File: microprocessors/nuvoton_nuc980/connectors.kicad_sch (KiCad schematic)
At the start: 9 parts, among them J10 Pmod UART 1x06 socket, J12 Pmod GPIO 1x06 socket, J13 Pmod GPIO 2x06 socket, J4 Pmod UART 1x06 socket, J5 Pmod SPI 1x06 socket, J6 Pmod GPIO 2x06 socket, J7 Pmod I2S 2x06 socket, J8 Pmod I2C 1x06 socket, J9 Conn_01x10

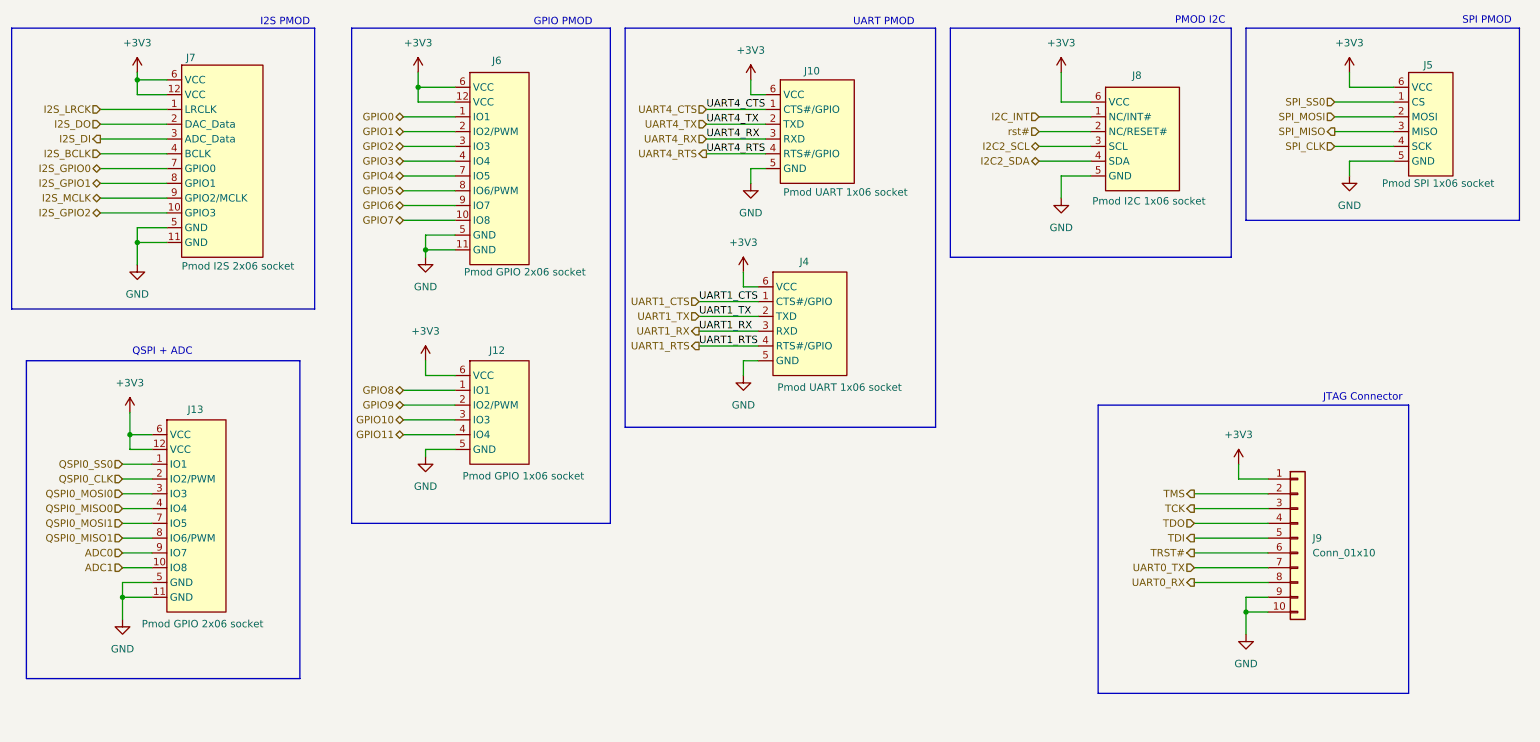
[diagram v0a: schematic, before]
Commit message: feat: ERC passing cotti-nuvoton
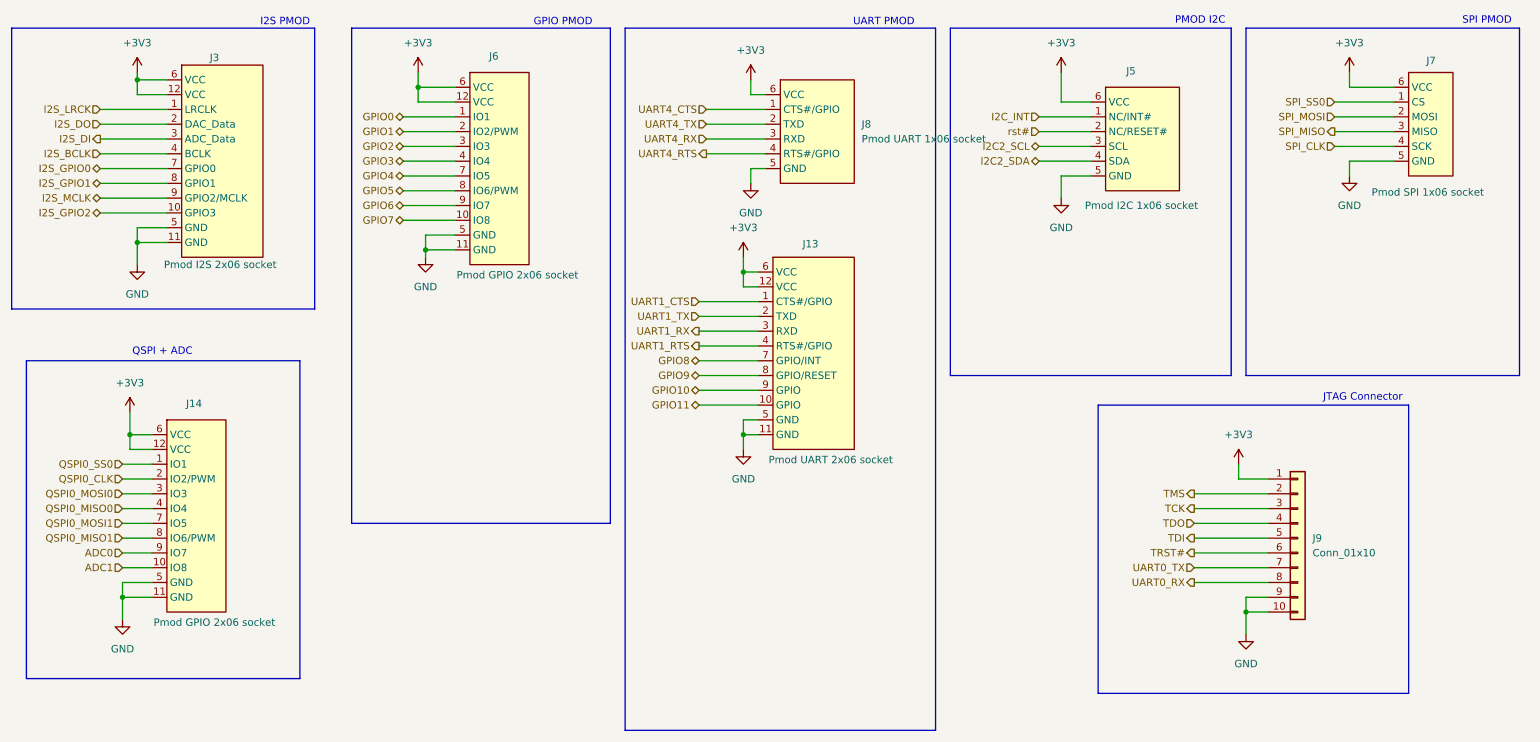
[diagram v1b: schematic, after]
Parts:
- removed J10, J4: Pmod UART 1x06 socket, Pmod:Pmod_1x06_socket, symbol Pmod:pmod_uart_1x06_socket
- removed J12: Pmod GPIO 1x06 socket, Pmod:Pmod_1x06_socket, symbol Pmod:pmod_gpio_1x06_socket
- removed J13, J6: Pmod GPIO 2x06 socket, Pmod:Pmod_2x06_socket, symbol Pmod:pmod_gpio_2x06_socket
- removed J5: Pmod SPI 1x06 socket, Pmod:Pmod_1x06_socket, symbol Pmod:pmod_spi_1x06_socket
- removed J7: Pmod I2S 2x06 socket, Pmod:Pmod_2x06_socket, symbol Pmod:pmod_i2s_2x06_socket
- removed J8: Pmod I2C 1x06 socket, Pmod:Pmod_1x06_socket, symbol Pmod:pmod_i2c_1x06_socket
- added J13: Pmod UART 2x06 socket, cotti_footprints:Pmod_2x06_socket, symbol cotti_pmod:pmod_uart_2x06_socket
- added J14, J6: Pmod GPIO 2x06 socket, cotti_footprints:Pmod_2x06_socket, symbol cotti_pmod:pmod_gpio_2x06_socket
- added J3: Pmod I2S 2x06 socket, cotti_footprints:Pmod_2x06_socket, symbol cotti_pmod:pmod_i2s_2x06_socket
- added J5: Pmod I2C 1x06 socket, cotti_footprints:Pmod_1x06_socket, symbol cotti_pmod:pmod_i2c_1x06_socket
- added J7: Pmod SPI 1x06 socket, cotti_footprints:Pmod_1x06_socket, symbol cotti_pmod:pmod_spi_1x06_socket
- added J8: Pmod UART 1x06 socket, cotti_footprints:Pmod_1x06_socket, symbol cotti_pmod:pmod_uart_1x06_socket
- J9: footprint (none) -> Connector_PinHeader_2.54mm:PinHeader_1x10_P2.54mm_Vertical
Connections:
- net +3V3: now also J13.12 (VCC), J13.6 (VCC), J14.12 (VCC), J14.6 (VCC), J3.12 (VCC), J3.6 (VCC), J5.6 (VCC), J6.12 (VCC), J6.6 (VCC), J7.6 (VCC), J8.6 (VCC)
- net ADC0: now also J14.9 (IO7)
- net ADC1: now also J14.10 (IO8)
- net GND: now also J13.11 (GND), J13.5 (GND), J14.11 (GND), J14.5 (GND), J3.11 (GND), J3.5 (GND), J5.5 (GND), J6.11 (GND), J6.5 (GND), J7.5 (GND), J8.5 (GND)
- net GPIO0: now also J6.1 (IO1)
- net GPIO1: now also J6.2 (IO2/PWM)
- net GPIO10: now also J13.9 (GPIO)
- net GPIO11: now also J13.10 (GPIO)
- net GPIO2: now also J6.3 (IO3)
- net GPIO3: now also J6.4 (IO4)
- net GPIO4: now also J6.7 (IO5)
- net GPIO5: now also J6.8 (IO6/PWM)
- net GPIO6: now also J6.9 (IO7)
- net GPIO7: now also J6.10 (IO8)
- net GPIO8: now also J13.7 (GPIO/INT)
- net GPIO9: now also J13.8 (GPIO/RESET)
- net I2C2_SCL: now also J5.3 (SCL)
- net I2C2_SDA: now also J5.4 (SDA)
- net I2C_INT: now also J5.1 (NC/INT#)
- net I2S_BCLK: now also J3.4 (BCLK)
- net I2S_DI: now also J3.3 (ADC_Data)
- net I2S_DO: now also J3.2 (DAC_Data)
- net I2S_GPIO0: now also J3.7 (GPIO0)
- net I2S_GPIO1: now also J3.8 (GPIO1)
- net I2S_GPIO2: now also J3.10 (GPIO3)
- net I2S_LRCK: now also J3.1 (LRCLK)
- net I2S_MCLK: now also J3.9 (GPIO2/MCLK)
- net QSPI0_CLK: now also J14.2 (IO2/PWM)
- net QSPI0_MISO0: now also J14.4 (IO4)
- net QSPI0_MISO1: now also J14.8 (IO6/PWM)
- net QSPI0_MOSI0: now also J14.3 (IO3)
- net QSPI0_MOSI1: now also J14.7 (IO5)
- net QSPI0_SS0: now also J14.1 (IO1)
- net SPI_CLK: now also J7.4 (SCK)
- net SPI_MISO: now also J7.3 (MISO)
- net SPI_MOSI: now also J7.2 (MOSI)
- net SPI_SS0: now also J7.1 (CS)
- net UART1_CTS: now also J13.1 (CTS#/GPIO)
- net UART1_RTS: now also J13.4 (RTS#/GPIO)
- net UART1_RX: now also J13.3 (RXD)
- net UART1_TX: now also J13.2 (TXD)
- net UART4_CTS: now also J8.1 (CTS#/GPIO)
- net UART4_RTS: now also J8.4 (RTS#/GPIO)
- net UART4_RX: now also J8.3 (RXD)
- net UART4_TX: now also J8.2 (TXD)
- net rst#: now also J5.2 (NC/RESET#)
